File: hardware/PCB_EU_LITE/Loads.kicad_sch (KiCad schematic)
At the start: 15 parts, among them J701 PTC + / RETURN, J702 PUMP + / RETURN, Q701 BC847B-DIO, Q702 BC857B, Q703 BSC146N10LS5, Q704 AO3422

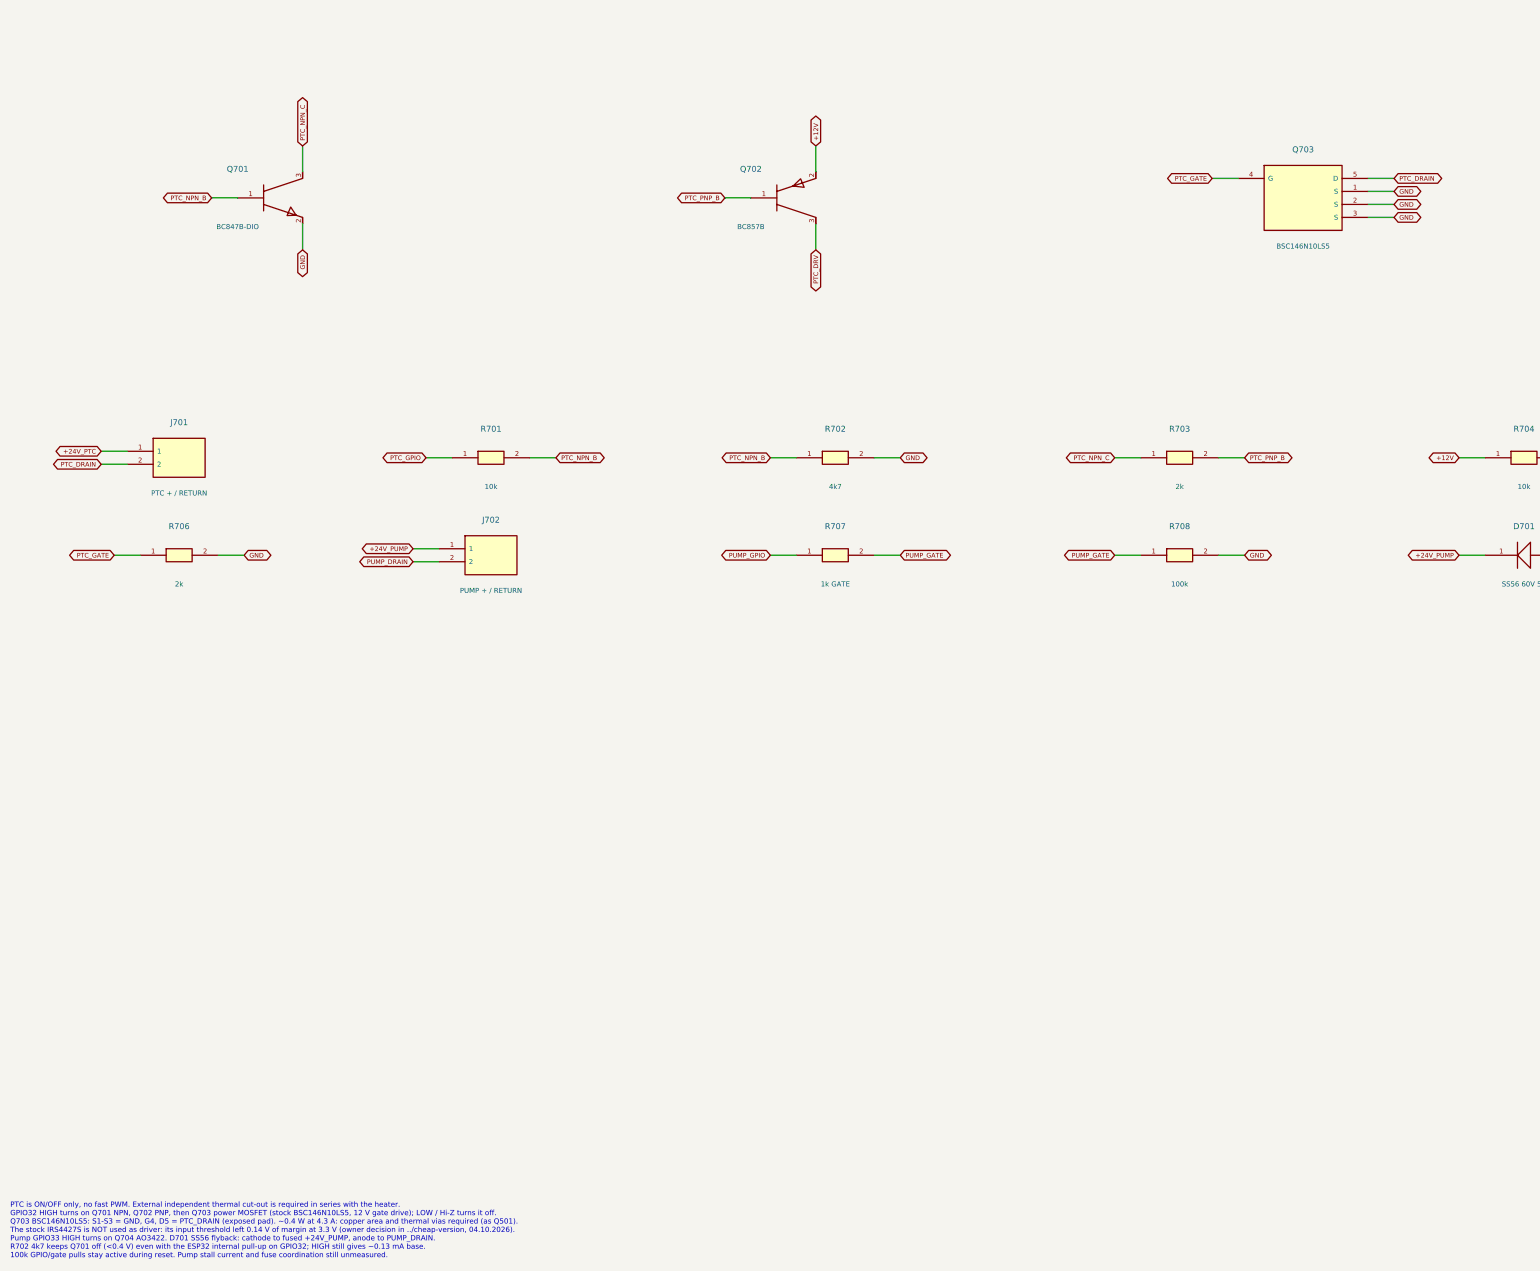
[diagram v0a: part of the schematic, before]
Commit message: Replace EU-LITE PTC MOSFET with TO-220 part
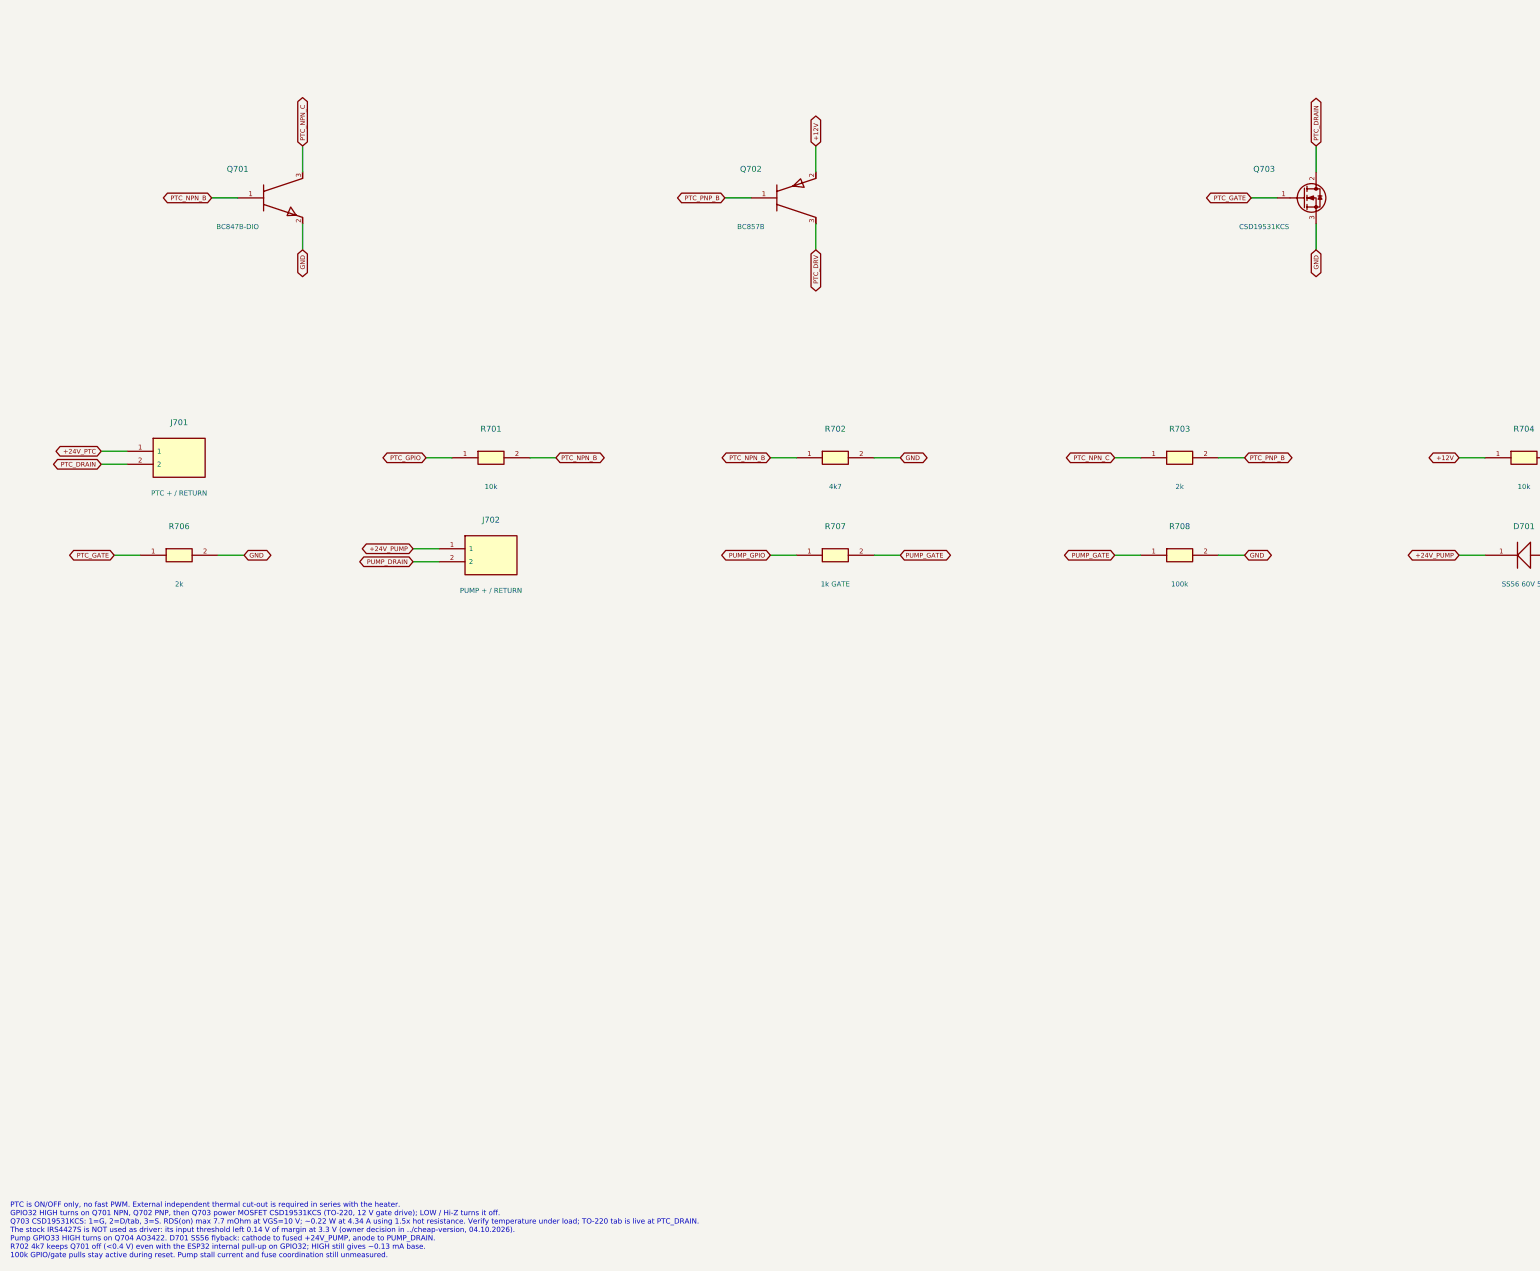
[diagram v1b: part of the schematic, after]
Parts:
- Q703: value BSC146N10LS5 -> CSD19531KCS; footprint Package_TO_SOT_SMD:TDSON-8-1 -> Package_TO_SOT_THT:TO-220-3_Vertical; symbol EU_LITE:NMOS_SO8 -> EU_LITE:NMOS; Design_note Stock BSC146N10LS5 (second and last piece) -> Salvats catalog snapshot 2026-10-23; TI datasheet: 100 V, T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; FootprintStatus DRAWING CHECKED in EU-0.1/cheap-version - physical fit pend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 -> PACKAGE ONLY - verify before PCB; MPN BSC146N10LS5 -> CSD19531KCS; Source stock:112 -> buy
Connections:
- net GND: no longer Q703.1 (S), Q703.2 (S)
- net PTC_DRAIN: now also Q703.2 (D); no longer Q703.5 (D)
- net PTC_GATE: now also Q703.1 (G); no longer Q703.4 (G)
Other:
- note added: "PTC is ON/OFF only, no fast PWM. External independent thermal cut-out is required in series with the heater. GPIO32 HIGH turns on Q701 NPN, Q702 PNP, then Q703 power MOSFET CSD19531KCS (TO-220, 12 V gate drive); LOW / Hi-Z turns it off. Q703 CSD19531KCS: 1=G, 2=D/tab, 3=S. RDS(on) max 7.7 mOhm at VGS=10 V; ~0.22 W at 4.34 A using 1.5x hot resistance. Verify temperature under load; TO-220 tab is l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"
- note removed: "PTC is ON/OFF only, no fast PWM. External independent thermal cut-out is required in series with the heater. GPIO32 HIGH turns on Q701 NPN, Q702 PNP, then Q703 power MOSFET (stock BSC146N10LS5, 12 V gate drive); LOW / Hi-Z turns it off. Q703 BSC146N10LS5: S1-S3 = GND, G4, D5 = PTC_DRAIN (exposed pad). ~0.4 W at 4.3 A: copper area and thermal vias required (as Q501). The stock IRS4427S is NOT used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"
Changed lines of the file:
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@@
 (kicad_sch (version 20260306) (generator "eeschema") (generator_version "10.0") (paper "A3") (title_block (title "07 | PTC heater and 24 V pump") (date "2026-10-24") (rev "EU-LITE-0.1") (company "GrowBox | EU-LITE from stock") (comment 1 "SCHEMATIC DRAFT | no PCB / manufacturing release"))
 (text "07 | PTC heater and 24 V pump" (at 12.7 12.7 0) (effects (font (size 2 2)) (justify left top)))
-(text "PTC is ON/OFF only, no fast PWM. External independent thermal cut-out is required in series with the heater.\nGPIO32 HIGH turns on Q701 NPN, Q702 PNP, then Q703 power MOSFET (stock BSC146N10LS5, 12 V gate drive); LOW / Hi-Z turns it off.\nQ703 BSC146N10LS5: S1-S3 = GND, G4, D5 = PTC_DRAIN (exposed pad). ~0.4 W at 4.3 A: copper area and thermal vias required (as Q501).\nThe stock IRS4427S is NOT used as driver: its input threshold left 0.14 V of margin at 3.3 V (owner decision in ../cheap-version, 04.10.2026).\nPump GPIO33 HIGH turns on Q704 AO3422. D701 SS56 flyback: cathode to fused +24V_PUMP, anode to PUMP_DRAIN.\nR702 4k7 keeps Q701 off (<0.4 V) even with the ESP32 internal pull-up on GPIO32; HIGH still gives ~0.13 mA base.\n100k GPIO/gate pulls stay active during reset. Pump stall current and fuse coordination still unmeasured." (at 12.7 251 0) (effects (font (size 1.02 1.02)) (justify left top)))
+(text "PTC is ON/OFF only, no fast PWM. External independent thermal cut-out is required in series with the heater.\nGPIO32 HIGH turns on Q701 NPN, Q702 PNP, then Q703 power MOSFET CSD19531KCS (TO-220, 12 V gate drive); LOW / Hi-Z turns it off.\nQ703 CSD19531KCS: 1=G, 2=D/tab, 3=S. RDS(on) max 7.7 mOhm at VGS=10 V; ~0.22 W at 4.34 A using 1.5x hot resistance. Verify temperature under load; TO-220 tab is live at PTC_DRAIN.\nThe stock IRS4427S is NOT used as driver: its input threshold left 0.14 V of margin at 3.3 V (owner decision in ../cheap-version, 04.10.2026).\nPump GPIO33 HIGH turns on Q704 AO3422. D701 SS56 flyback: cathode to fused +24V_PUMP, anode to PUMP_DRAIN.\nR702 4k7 keeps Q701 off (<0.4 V) even with the ESP32 internal pull-up on GPIO32; HIGH still gives ~0.13 mA base.\n100k GPIO/gate pulls stay active during reset. Pump stall current and fuse coordination still unmeasured." (at 12.7 251 0) (effects (font (size 1.02 1.02)) (justify left top)))
 (symbol (lib_id "EU_LITE:J2") (at 45.72 105.41 0) (unit 1) (in_bom yes) (on_board yes) (dnp no)
 (property "Reference" "J701" (at 45.72 98.5 0) (effects (font (size 1.15 1.15)) ))
@@
 (wire (pts (xy 170.18 59.69) (xy 170.18 64.77)) (stroke (width 0) (type default)))
 (global_label "PTC_DRV" (shape bidirectional) (at 170.18 64.77 270) (effects (font (size 0.9 0.9)) (justify right)) (property "Intersheetrefs" "${INTERSHEET_REFS}" (at 170.18 64.77 0) (effects (font (size 1 1)) (hide yes))))
-(symbol (lib_id "EU_LITE:NMOS_SO8") (at 265.43 54.61 0) (unit 1) (in_bom yes) (on_board yes) (dnp no)
-(property "Reference" "Q703" (at 265.43 45.16 0) (effects (font (size 1.15 1.15)) ))
-(property "Value" "BSC146N10LS5" (at 265.43 64.06 0) (effects (font (size 0.98 0.98)) ))
-(property "Footprint" "Package_TO_SOT_SMD:TDSON-8-1" (at 265.43 54.61 0) (effects (font (size 1 1)) (hide yes)))
-(property "Datasheet" "https://www.infineon.com/dgdl/Infineon-BSC146N10LS5-DS-v02_00-EN.pdf" (at 265.43 54.61 0) (effects (font (size 1 1)) (hide yes)))
-(property "MPN" "BSC146N10LS5" (at 265.43 54.61 0) (effects (font (size 1 1)) (hide yes)))
-(property "Source" "stock:112" (at 265.43 54.61 0) (effects (font (size 1 1)) (hide yes)))
-(property "Design_note" "Stock BSC146N10LS5 (second and last piece)" (at 265.43 54.61 0) (effects (font (size 1 1)) (hide yes)))
-(property "FootprintStatus" "DRAWING CHECKED in EU-0.1/cheap-version - physical fit pending" (at 265.43 54.61 0) (effects (font (size 1 1)) (hide yes)))
-(pin "4")
-(pin "5")
+(symbol (lib_id "EU_LITE:NMOS") (at 265.43 54.61 0) (unit 1) (in_bom yes) (on_board yes) (dnp no)
+(property "Reference" "Q703" (at 257.81 48.97 0) (effects (font (size 1.15 1.15)) ))
+(property "Value" "CSD19531KCS" (at 257.81 60.25 0) (effects (font (size 0.98 0.98)) ))
+(property "Footprint" "Package_TO_SOT_THT:TO-220-3_Vertical" (at 265.43 54.61 0) (effects (font (size 1 1)) (hide yes)))
+(property "Datasheet" "https://www.ti.com/lit/ds/symlink/csd19531kcs.pdf" (at 265.43 54.61 0) (effects (font (size 1 1)) (hide yes)))
+(property "MPN" "CSD19531KCS" (at 265.43 54.61 0) (effects (font (size 1 1)) (hide yes)))
+(property "Source" "buy" (at 265.43 54.61 0) (effects (font (size 1 1)) (hide yes)))
+(property "Design_note" "Salvats catalog snapshot 2026-10-23; TI datasheet: 100 V, TO-220, RDS(on) max 7.7 mOhm at VGS=10 V. Tab = drain; ~0.22 W at 4.34 A with 1.5x hot-resistance estimate. Check physical temperature; insulate live tab from grounded heatsink." (at 265.43 54.61 0) (effects (font (size 1 1)) (hide yes)))
+(property "FootprintStatus" "PACKAGE ONLY - verify before PCB" (at 265.43 54.61 0) (effects (font (size 1 1)) (hide yes)))
 (pin "1")
 (pin "2")
 (pin "3")
 (instances (project "PCB_EU_LITE" (path "/6650c329-4f4f-5b7a-a019-ee8e8f2772e1/c30ecf18-b1b2-59a9-9724-01d4f444e536" (reference "Q703") (unit 1)))) )
-(wire (pts (xy 252.73 50.8) (xy 247.65 50.8)) (stroke (width 0) (type default)))
-(global_label "PTC_GATE" (shape bidirectional) (at 247.65 50.8 180) (effects (font (size 0.9 0.9)) (justify right)) (property "Intersheetrefs" "${INTERSHEET_REFS}" (at 247.65 50.8 0) (effects (font (size 1 1)) (hide yes))))
-(wire (pts (xy 278.13 50.8) (xy 283.21 50.8)) (stroke (width 0) (type default)))
-(global_label "PTC_DRAIN" (shape bidirectional) (at 283.21 50.8 0) (effects (font (size 0.9 0.9)) (justify left)) (property "Intersheetrefs" "${INTERSHEET_REFS}" (at 283.21 50.8 0) (effects (font (size 1 1)) (hide yes))))
-(wire (pts (xy 278.13 53.34) (xy 283.21 53.34)) (stroke (width 0) (type default)))
-(global_label "GND" (shape bidirectional) (at 283.21 53.34 0) (effects (font (size 0.9 0.9)) (justify left)) (property "Intersheetrefs" "${INTERSHEET_REFS}" (at 283.21 53.34 0) (effects (font (size 1 1)) (hide yes))))
-(wire (pts (xy 278.13 55.88) (xy 283.21 55.88)) (stroke (width 0) (type default)))
-(global_label "GND" (shape bidirectional) (at 283.21 55.88 0) (effects (font (size 0.9 0.9)) (justify left)) (property "Intersheetrefs" "${INTERSHEET_REFS}" (at 283.21 55.88 0) (effects (font (size 1 1)) (hide yes))))
-(wire (pts (xy 278.13 58.42) (xy 283.21 58.42)) (stroke (width 0) (type default)))
-(global_label "GND" (shape bidirectional) (at 283.21 58.42 0) (effects (font (size 0.9 0.9)) (justify left)) (property "Intersheetrefs" "${INTERSHEET_REFS}" (at 283.21 58.42 0) (effects (font (size 1 1)) (hide yes))))
+(wire (pts (xy 260.35 54.61) (xy 255.27 54.61)) (stroke (width 0) (type default)))
+(global_label "PTC_GATE" (shape bidirectional) (at 255.27 54.61 180) (effects (font (size 0.9 0.9)) (justify right)) (property "Intersheetrefs" "${INTERSHEET_REFS}" (at 255.27 54.61 0) (effects (font (size 1 1)) (hide yes))))
+(wire (pts (xy 267.97 49.53) (xy 267.97 44.45)) (stroke (width 0) (type default)))
+(global_label "PTC_DRAIN" (shape bidirectional) (at 267.97 44.45 90) (effects (font (size 0.9 0.9)) (justify left)) (property "Intersheetrefs" "${INTERSHEET_REFS}" (at 267.97 44.45 0) (effects (font (size 1 1)) (hide yes))))
+(wire (pts (xy 267.97 59.69) (xy 267.97 64.77)) (stroke (width 0) (type default)))
+(global_label "GND" (shape bidirectional) (at 267.97 64.77 270) (effects (font (size 0.9 0.9)) (justify right)) (property "Intersheetrefs" "${INTERSHEET_REFS}" (at 267.97 64.77 0) (effects (font (size 1 1)) (hide yes))))
 (symbol (lib_id "EU_LITE:R") (at 106.68 105.41 0) (unit 1) (in_bom yes) (on_board yes) (dnp no)
 (property "Reference" "R701" (at 106.68 99.77 0) (effects (font (size 1.15 1.15)) ))
